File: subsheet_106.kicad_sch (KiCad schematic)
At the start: 2 parts, among them U402 32.215905 MHz (NTSC) — 32.084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

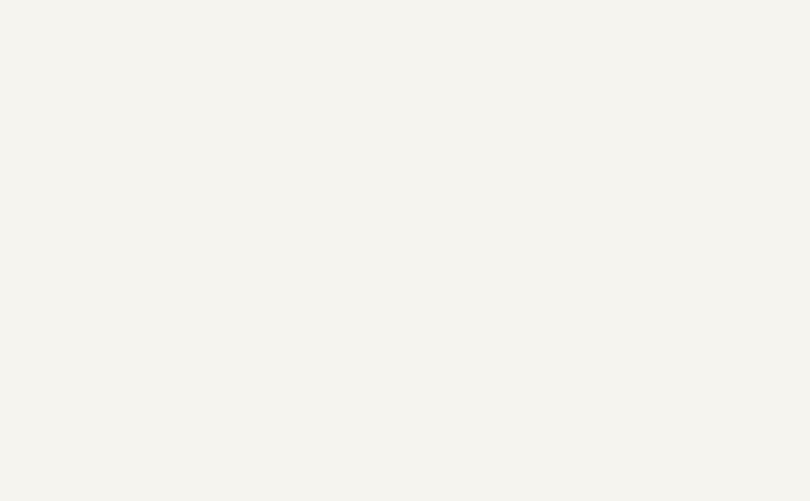
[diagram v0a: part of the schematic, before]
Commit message: add gnd/vcc symbol to start replacing local labels
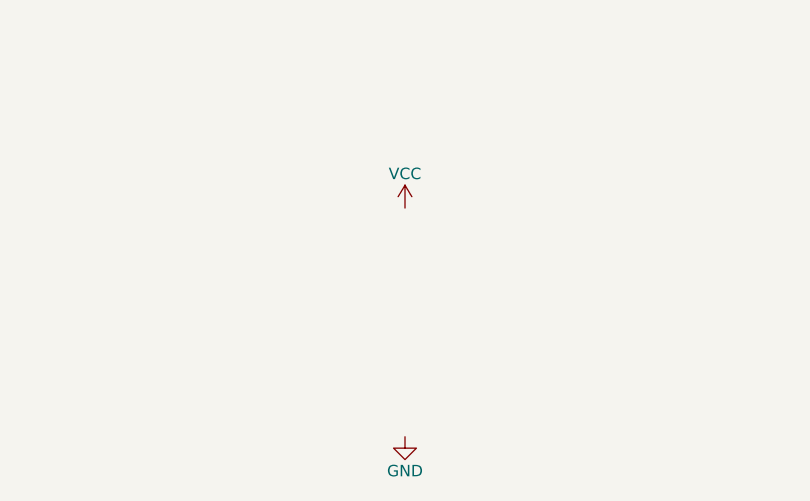
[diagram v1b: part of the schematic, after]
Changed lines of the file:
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@@
     (pin "2")
   )
+  (symbol (lib_id "power:GND") (at 158.75 190.5 0) (unit 1)
+    (in_bom yes) (on_board yes)
+    (property "Reference" "#PWR?" (id 0) (at 158.75 196.85 0)
+      (effects (font (size 1.27 1.27)) hide)
+    )
+    (property "Value" "GND" (id 1) (at 158.75 194.31 0))
+    (property "Footprint" "" (id 2) (at 158.75 190.5 0)
+      (effects (font (size 1.27 1.27)) hide)
+    )
+    (property "Datasheet" "" (id 3) (at 158.75 190.5 0)
+      (effects (font (size 1.27 1.27)) hide)
+    )
+    (pin "1")
+  )
+  (symbol (lib_id "power:VCC") (at 158.75 165.1 0) (unit 1)
+    (in_bom yes) (on_board yes)
+    (property "Reference" "#PWR?" (id 0) (at 158.75 168.91 0)
+      (effects (font (size 1.27 1.27)) hide)
+    )
+    (property "Value" "VCC" (id 1) (at 158.75 161.29 0))
+    (property "Footprint" "" (id 2) (at 158.75 165.1 0)
+      (effects (font (size 1.27 1.27)) hide)
+    )
+    (property "Datasheet" "" (id 3) (at 158.75 165.1 0)
+      (effects (font (size 1.27 1.27)) hide)
+    )
+    (pin "1")
+  )
 )
